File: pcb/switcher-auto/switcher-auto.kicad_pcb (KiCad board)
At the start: 2 copper layers, 151.8 x 46 mm, 26 parts, among them J1 Conn_02x22_Top_Bottom, J10 MD-90SM, J11 MD-90SM, J12 MD-90SM, J13 MD-90SM, J14 MD-90SM, J15 Conn_02x22_Top_Bottom, J2 Conn_02x22_Top_Bottom, J3 Conn_02x22_Top_Bottom, J4 MD-90SM, SW1 SW_Push, SW2 SW_Push, U1 CD74HC4067SM96, U2 CD74HC4067SM96, U3 CD74HC4067SM96, U4 CD74HC4067SM96, U5 CD74HC4067SM96, U6 CD74HC4067SM96, U7 CD74HC4067SM96

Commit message: WIP routing as 4 layers with new connector organization
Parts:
- J1: value Conn_02x22_Top_Bottom -> MD-90SM; footprint connector:REB_PinHeader_2x20_P1.27mm_Vertical_Renumbered -> DIN9:CUI_MD-90SM
- J15: footprint Connector_PinSocket_1.27mm:PinSocket_2x20_P1.27mm_Vertical -> connector:REB_PinHeader_2x20_P1.27mm_Vertical_Renumbered
- J4: value MD-90SM -> Conn_02x22_Top_Bottom; footprint DIN9:CUI_MD-90SM -> connector:REB_PinHeader_2x20_P1.27mm_Vertical_Renumbered
- moved J14 165.4 mm to (210.0, 137.9)
- moved J13 135.8 mm to (180.5, 137.9)
- moved J1 132.8 mm to (211.0, 76.9), turned to 0 degrees
- moved J12 108.7 mm to (151.0, 137.9)
- moved J11 86.3 mm to (121.5, 137.9)
- moved J15 85.3 mm to (137.9, 118.6)
- moved J4 57.1 mm to (164.9, 42.6), turned to 90 degrees
- moved J10 53.4 mm to (92.0, 137.9)
- moved J2 41.6 mm to (83.9, 42.6)
- moved J3 39.5 mm to (124.4, 42.6)
- moved U4 5.36 mm to (179.0, 58.0)
- moved B1 5.22 mm to (215.0, 44.0)
- moved H2 3.58 mm to (75.0, 75.0)
- moved H4 3.54 mm to (225.0, 75.0)
- moved H1 2.17 mm to (75.0, 55.0)
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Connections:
- net /15_5V renamed /15_VCC
- net /SEL_5V renamed /SEL_VCC
- J1 pad 1: /0_BVID -> /SEL_BVID
- J1 pad 2: /0_GVID -> /VCC
- J1 pad 3: /0_RVID -> /SEL_GVID
- J1 pad 4: /0_CVID -> /SEL_CVID
- J1 pad 5: /0_LAUD -> unconnected-(J1-CSYNC-Pad5)
- J1 pad 6: /0_RAUD -> unconnected-(J1-MAUD-Pad6)
- J1 pad 7: /0_5V -> /SEL_RVID
- J1 pad 8: GND -> /SEL_LAUD
- J1 pad 9: /1_BVID -> /SEL_RAUD
- J10 pad 2: /Daughterboard/0_5V -> /Daughterboard/0_VCC
- J11 pad 2: /Daughterboard/1_5V -> /Daughterboard/1_VCC
- J11 pad S1: /Daughterboard/1_GND -> /Daughterboard/0_GND
- J11 pad S2: /Daughterboard/1_GND -> /Daughterboard/0_GND
- J11 pad S3: /Daughterboard/1_GND -> /Daughterboard/0_GND
- J12 pad 2: /Daughterboard/2_5V -> /Daughterboard/2_VCC
- J12 pad S1: /Daughterboard/2_GND -> /Daughterboard/0_GND
- J12 pad S2: /Daughterboard/2_GND -> /Daughterboard/0_GND
- J12 pad S3: /Daughterboard/2_GND -> /Daughterboard/0_GND
- J13 pad 2: /Daughterboard/3_5V -> /Daughterboard/3_VCC
- J13 pad S1: /Daughterboard/3_GND -> /Daughterboard/0_GND
- J13 pad S2: /Daughterboard/3_GND -> /Daughterboard/0_GND
- J13 pad S3: /Daughterboard/3_GND -> /Daughterboard/0_GND
- J14 pad 2: /Daughterboard/4_5V -> /Daughterboard/4_VCC
- J14 pad S1: /Daughterboard/4_GND -> /Daughterboard/0_GND
- J14 pad S2: /Daughterboard/4_GND -> /Daughterboard/0_GND
- J14 pad S3: /Daughterboard/4_GND -> /Daughterboard/0_GND
- J15 pad 1: /Daughterboard/0_BVID -> /Daughterboard/0_RVID
- J15 pad 10: /Daughterboard/1_GVID -> /Daughterboard/4_BVID
- J15 pad 11: /Daughterboard/1_RVID -> /Daughterboard/0_GVID
- J15 pad 12: /Daughterboard/1_CVID -> /Daughterboard/1_GVID
- J15 pad 13: /Daughterboard/1_LAUD -> /Daughterboard/2_GVID
- J15 pad 14: /Daughterboard/1_RAUD -> /Daughterboard/3_GVID
- J15 pad 15: /Daughterboard/1_5V -> /Daughterboard/4_GVID
- J15 pad 16: /Daughterboard/1_GND -> /Daughterboard/0_GND
- J15 pad 17: /Daughterboard/4_BVID -> /Daughterboard/0_GND
- J15 pad 18: /Daughterboard/4_GVID -> /Daughterboard/0_GND
- J15 pad 19: /Daughterboard/4_RVID -> /Daughterboard/0_GND
- J15 pad 2: /Daughterboard/0_GVID -> /Daughterboard/1_RVID
- J15 pad 20: /Daughterboard/4_CVID -> /Daughterboard/0_GND
- J15 pad 21: /Daughterboard/4_LAUD -> /Daughterboard/0_VCC
- J15 pad 22: /Daughterboard/4_RAUD -> /Daughterboard/1_VCC
- J15 pad 23: /Daughterboard/4_5V -> /Daughterboard/2_VCC
- J15 pad 24: /Daughterboard/4_GND -> /Daughterboard/3_VCC
- J15 pad 25: /Daughterboard/3_BVID -> /Daughterboard/4_VCC
- J15 pad 26: /Daughterboard/3_GVID -> /Daughterboard/0_RAUD
- J15 pad 27: /Daughterboard/3_RVID -> /Daughterboard/1_RAUD
- J15 pad 28: /Daughterboard/3_CVID -> /Daughterboard/2_RAUD
- J15 pad 29: /Daughterboard/3_LAUD -> /Daughterboard/3_RAUD
- J15 pad 3: /Daughterboard/0_RVID -> /Daughterboard/2_RVID
- J15 pad 30: /Daughterboard/3_RAUD -> /Daughterboard/4_RAUD
- J15 pad 31: /Daughterboard/3_5V -> /Daughterboard/0_LAUD
- J15 pad 32: /Daughterboard/3_GND -> /Daughterboard/1_LAUD
- J15 pad 33: /Daughterboard/2_BVID -> /Daughterboard/2_LAUD
- J15 pad 34: /Daughterboard/2_GVID -> /Daughterboard/3_LAUD
- J15 pad 35: /Daughterboard/2_RVID -> /Daughterboard/4_LAUD
- J15 pad 36: /Daughterboard/2_CVID -> /Daughterboard/0_CVID
- J15 pad 37: /Daughterboard/2_LAUD -> /Daughterboard/1_CVID
- J15 pad 38: /Daughterboard/2_RAUD -> /Daughterboard/2_CVID
- J15 pad 39: /Daughterboard/2_5V -> /Daughterboard/3_CVID
- J15 pad 4: /Daughterboard/0_CVID -> /Daughterboard/3_RVID
- J15 pad 40: /Daughterboard/2_GND -> /Daughterboard/4_CVID
- J15 pad 5: /Daughterboard/0_LAUD -> /Daughterboard/4_RVID
- J15 pad 6: /Daughterboard/0_RAUD -> /Daughterboard/0_BVID
- J15 pad 7: /Daughterboard/0_5V -> /Daughterboard/1_BVID
- J15 pad 8: /Daughterboard/0_GND -> /Daughterboard/2_BVID
- J15 pad 9: /Daughterboard/1_BVID -> /Daughterboard/3_BVID
- J2 pad 1: /5_BVID -> /0_RVID
- J2 pad 10: /6_GVID -> /4_BVID
- J2 pad 11: /6_RVID -> /0_GVID
- J2 pad 12: /6_CVID -> /1_GVID
- J2 pad 13: /6_LAUD -> /2_GVID
- J2 pad 14: /6_RAUD -> /3_GVID
- J2 pad 15: /6_5V -> /4_GVID
- J2 pad 17: /9_BVID -> GND
- J2 pad 18: /9_GVID -> GND
- J2 pad 19: /9_RVID -> GND
- J2 pad 2: /5_GVID -> /1_RVID
- J2 pad 20: /9_CVID -> GND
- J2 pad 21: /9_LAUD -> /0_VCC
- J2 pad 22: /9_RAUD -> /1_VCC
- J2 pad 23: /9_5V -> /2_VCC
- J2 pad 24: GND -> /3_VCC
- J2 pad 25: /8_BVID -> /4_VCC
- J2 pad 26: /8_GVID -> /0_RAUD
- J2 pad 27: /8_RVID -> /1_RAUD
- J2 pad 28: /8_CVID -> /2_RAUD
- J2 pad 29: /8_LAUD -> /3_RAUD
- J2 pad 3: /5_RVID -> /2_RVID
- J2 pad 30: /8_RAUD -> /4_RAUD
- J2 pad 31: /8_5V -> /0_LAUD
- J2 pad 32: GND -> /1_LAUD
- J2 pad 33: /7_BVID -> /2_LAUD
- J2 pad 34: /7_GVID -> /3_LAUD
- J2 pad 35: /7_RVID -> /4_LAUD
- J2 pad 36: /7_CVID -> /0_CVID
- J2 pad 37: /7_LAUD -> /1_CVID
- J2 pad 38: /7_RAUD -> /2_CVID
- J2 pad 39: /7_5V -> /3_CVID
- J2 pad 4: /5_CVID -> /3_RVID
- J2 pad 40: GND -> /4_CVID
- J2 pad 5: /5_LAUD -> /4_RVID
- J2 pad 6: /5_RAUD -> /0_BVID
- J2 pad 7: /5_5V -> /1_BVID
- J2 pad 8: GND -> /2_BVID
- J2 pad 9: /6_BVID -> /3_BVID
- J3 pad 1: /10_BVID -> /5_RVID
- J3 pad 10: /11_GVID -> /9_BVID
- J3 pad 11: /11_RVID -> /5_GVID
- J3 pad 12: /11_CVID -> /6_GVID
- J3 pad 13: /11_LAUD -> /7_GVID
- J3 pad 14: /11_RAUD -> /8_GVID
- J3 pad 15: /11_5V -> /9_GVID
- J3 pad 17: /14_BVID -> GND
- J3 pad 18: /14_GVID -> GND
- J3 pad 19: /14_RVID -> GND
- J3 pad 2: /10_GVID -> /6_RVID
- J3 pad 20: /14_CVID -> GND
- J3 pad 21: /14_LAUD -> /5_VCC
- J3 pad 22: /14_RAUD -> /6_VCC
- J3 pad 23: /14_5V -> /7_VCC
- J3 pad 24: GND -> /8_VCC
- J3 pad 25: /13_BVID -> /9_VCC
- J3 pad 26: /13_GVID -> /5_RAUD
- J3 pad 27: /13_RVID -> /6_RAUD
- J3 pad 28: /13_CVID -> /7_RAUD
- J3 pad 29: /13_LAUD -> /8_RAUD
- J3 pad 3: /10_RVID -> /7_RVID
- J3 pad 30: /13_RAUD -> /9_RAUD
- J3 pad 31: /13_5V -> /5_LAUD
- J3 pad 32: GND -> /6_LAUD
- J3 pad 33: /12_BVID -> /7_LAUD
- J3 pad 34: /12_GVID -> /8_LAUD
- J3 pad 35: /12_RVID -> /9_LAUD
- J3 pad 36: /12_CVID -> /5_CVID
- J3 pad 37: /12_LAUD -> /6_CVID
- J3 pad 38: /12_RAUD -> /7_CVID
- J3 pad 39: /12_5V -> /8_CVID
- J3 pad 4: /10_CVID -> /8_RVID
- J3 pad 40: GND -> /9_CVID
- J3 pad 5: /10_LAUD -> /9_RVID
- J3 pad 6: /10_RAUD -> /5_BVID
- J3 pad 7: /10_5V -> /6_BVID
- J3 pad 8: GND -> /7_BVID
- J3 pad 9: /11_BVID -> /8_BVID
- J4 pad 1: /SEL_BVID -> /10_RVID
- J4 pad 2: /VCC -> /11_RVID
- J4 pad 3: /SEL_GVID -> /12_RVID
- J4 pad 4: /SEL_CVID -> /13_RVID
- J4 pad 5: unconnected-(J4-CSYNC-Pad5) -> /14_RVID
- J4 pad 6: unconnected-(J4-MAUD-Pad6) -> /10_BVID
- J4 pad 7: /SEL_RVID -> /11_BVID
- J4 pad 8: /SEL_LAUD -> /12_BVID
- J4 pad 9: /SEL_RAUD -> /13_BVID
- U1 pad 1: /SEL_BVID -> /SEL_RVID
- U1 pad 16: /15_BVID -> /15_RVID
- U1 pad 17: /14_BVID -> /14_RVID
- U1 pad 18: /13_BVID -> /13_RVID
- U1 pad 19: /12_BVID -> /12_RVID
- U1 pad 2: /7_BVID -> /7_RVID
- U1 pad 20: /11_BVID -> /11_RVID
- U1 pad 21: /10_BVID -> /10_RVID
- U1 pad 22: /9_BVID -> /9_RVID
- U1 pad 23: /8_BVID -> /8_RVID
- U1 pad 3: /6_BVID -> /6_RVID
- U1 pad 4: /5_BVID -> /5_RVID
- U1 pad 5: /4_BVID -> /4_RVID
- U1 pad 6: /3_BVID -> /3_RVID
- U1 pad 7: /2_BVID -> /2_RVID
- U1 pad 8: /1_BVID -> /1_RVID
- U1 pad 9: /0_BVID -> /0_RVID
- U2 pad 1: /SEL_GVID -> /SEL_BVID
- U2 pad 16: /15_GVID -> /15_BVID
- U2 pad 17: /14_GVID -> /14_BVID
- U2 pad 18: /13_GVID -> /13_BVID
- U2 pad 19: /12_GVID -> /12_BVID
- U2 pad 2: /7_GVID -> /7_BVID
- U2 pad 20: /11_GVID -> /11_BVID
- U2 pad 21: /10_GVID -> /10_BVID
- U2 pad 22: /9_GVID -> /9_BVID
- U2 pad 23: /8_GVID -> /8_BVID
- U2 pad 3: /6_GVID -> /6_BVID
- U2 pad 4: /5_GVID -> /5_BVID
- U2 pad 5: /4_GVID -> /4_BVID
- U2 pad 6: /3_GVID -> /3_BVID
- U2 pad 7: /2_GVID -> /2_BVID
- U2 pad 8: /1_GVID -> /1_BVID
- U2 pad 9: /0_GVID -> /0_BVID
- U3 pad 1: /SEL_RVID -> /SEL_GVID
- U3 pad 16: /15_RVID -> /15_GVID
- U3 pad 17: /14_RVID -> /14_GVID
- U3 pad 18: /13_RVID -> /13_GVID
- U3 pad 19: /12_RVID -> /12_GVID
- U3 pad 2: /7_RVID -> /7_GVID
- U3 pad 20: /11_RVID -> /11_GVID
- U3 pad 21: /10_RVID -> /10_GVID
- U3 pad 22: /9_RVID -> /9_GVID
- U3 pad 23: /8_RVID -> /8_GVID
- U3 pad 3: /6_RVID -> /6_GVID
- U3 pad 4: /5_RVID -> /5_GVID
- U3 pad 5: /4_RVID -> /4_GVID
- U3 pad 6: /3_RVID -> /3_GVID
- U3 pad 7: /2_RVID -> /2_GVID
- U3 pad 8: /1_RVID -> /1_GVID
- U3 pad 9: /0_RVID -> /0_GVID
- U7 pad 17: /14_5V -> /14_VCC
- U7 pad 18: /13_5V -> /13_VCC
- U7 pad 19: /12_5V -> /12_VCC
- U7 pad 2: /7_5V -> /7_VCC
- U7 pad 20: /11_5V -> /11_VCC
- U7 pad 21: /10_5V -> /10_VCC
- U7 pad 22: /9_5V -> /9_VCC
- U7 pad 23: /8_5V -> /8_VCC
- U7 pad 3: /6_5V -> /6_VCC
- U7 pad 4: /5_5V -> /5_VCC
- U7 pad 5: /4_5V -> /4_VCC
- U7 pad 6: /3_5V -> /3_VCC
- U7 pad 7: /2_5V -> /2_VCC
- U7 pad 8: /1_5V -> /1_VCC
- U7 pad 9: /0_5V -> /0_VCC
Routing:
- net /OE: track 0.00 -> 179.0 mm, vias 0 -> 4
- net /S0: track 0.00 -> 151.7 mm, vias 0 -> 2
- net /S2: track 0.00 -> 147.8 mm, vias 0 -> 2
- net /S1: track 0.00 -> 146.7 mm, vias 0 -> 2
- net /S3: track 0.00 -> 135.8 mm, vias 0 -> 3
- net /4_CVID: track 0.00 -> 107.2 mm, vias 0 -> 1
- net /10_LAUD: track 0.00 -> 107.1 mm, vias 0 -> 2
- net /3_CVID: track 0.00 -> 106.5 mm, vias 0 -> 1
- net /11_LAUD: track 0.00 -> 106.2 mm, vias 0 -> 2
- net /2_CVID: track 0.00 -> 105.7 mm, vias 0 -> 1
- net /12_LAUD: track 0.00 -> 105.2 mm, vias 0 -> 2
- net /1_CVID: track 0.00 -> 104.9 mm, vias 0 -> 1
- net /0_CVID: track 0.00 -> 104.2 mm, vias 0 -> 1
- net /13_LAUD: track 0.00 -> 104.0 mm, vias 0 -> 2
- net /14_LAUD: track 0.00 -> 102.9 mm, vias 0 -> 2
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- added copper zone on B.Cu, net /Daughterboard/0_GND
- added copper zone on F.Cu, net /Daughterboard/0_GND
- removed copper zone on B.Cu, net GND
- removed copper zone on F.Cu, net GND
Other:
- board size 151.8 x 46 mm -> 160 x 110 mm
- copper layers 2 -> 4

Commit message: Routing pt 2
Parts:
- added C1: 1u, Capacitor_SMD:C_0805_2012Metric_Pad1.18x1.45mm_HandSolder, F.Cu at (220.0, 63.0)
- added R3: R_Small, Resistor_SMD:R_1206_3216Metric_Pad1.30x1.75mm_HandSolder, F.Cu at (163.2, 130.8)
- added R4: R_Small, Resistor_SMD:R_1206_3216Metric_Pad1.30x1.75mm_HandSolder, F.Cu at (133.6, 130.8)
- added R5: R_Small, Resistor_SMD:R_1206_3216Metric_Pad1.30x1.75mm_HandSolder, F.Cu at (104.4, 130.8)
- added R6: 10K, Resistor_SMD:R_1206_3216Metric_Pad1.30x1.75mm_HandSolder, F.Cu at (209.9, 56.4)
- R1: value R -> R_Small
- R2: value 10K -> R_Small
- moved R1 75.8 mm to (222.2, 130.8), turned to 90 degrees
- moved R2 69.6 mm to (192.6, 130.8), turned to 90 degrees
- moved SW1 1.35 mm to (190.2, 73.0)
- moved SW2 1.27 mm to (179.5, 73.0)
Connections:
- B1 pad 17: unconnected-(B1-A0-Pad17) -> /SEL_VCC
- B1 pad 2: /OE -> unconnected-(B1-RXI-Pad2)
- B1 pad 5: /R0 -> /R1
- B1 pad 6: /R1 -> /R0
- B1 pad 7: /R2 -> /R3
- B1 pad 8: /R3 -> /R2
- B1 pad 9: Net-(B1-*6) -> unconnected-(B1-*6-Pad9)
- R1 pad 1: /SEL_VCC -> /Daughterboard/4_VCC
- R1 pad 2: Net-(B1-*6) -> unconnected-(R1-Pad2)
- R2 pad 1: Net-(B1-*6) -> /Daughterboard/3_VCC
- R2 pad 2: GND -> unconnected-(R2-Pad2)
- U1 pad 15: /OE -> GND
- U1 pad 16: /15_RVID -> unconnected-(U1-I15-Pad16)
- U2 pad 15: /OE -> GND
- U2 pad 16: /15_BVID -> unconnected-(U2-I15-Pad16)
- U3 pad 15: /OE -> GND
- U3 pad 16: /15_GVID -> unconnected-(U3-I15-Pad16)
- U4 pad 15: /OE -> GND
- U4 pad 16: /15_CVID -> unconnected-(U4-I15-Pad16)
- U5 pad 15: /OE -> GND
- U5 pad 16: /15_LAUD -> unconnected-(U5-I15-Pad16)
- U6 pad 15: /OE -> GND
- U6 pad 16: /15_RAUD -> unconnected-(U6-I15-Pad16)
- U7 pad 16: /15_VCC -> unconnected-(U7-I15-Pad16)
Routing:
- net /VCC: track 0.00 -> 288.8 mm, vias 0 -> 3
- net /OE: track 179.0 -> 0.00 mm, vias 4 -> 0
- net /SEL_RVID: track 0.00 -> 158.9 mm, vias 0 -> 1
- net /SEL_LAUD: track 0.00 -> 118.3 mm, vias 0 -> 1
- net /SEL_BVID: track 0.00 -> 113.6 mm, vias 0 -> 1
- net /SEL_GVID: track 0.00 -> 96.2 mm, vias 0 -> 1
- net /SEL_RAUD: track 0.00 -> 86.9 mm, vias 0 -> 1
- net /IE: track 0.00 -> 84.7 mm, vias 0 -> 1
- net /R1: track 0.00 -> 81.1 mm, vias 0 -> 1
- net /R0: track 0.00 -> 78.6 mm, vias 0 -> 1
- net /10_RAUD: track 0.00 -> 78.0 mm, vias 0 -> 1
- net /11_RAUD: track 0.00 -> 76.6 mm, vias 0 -> 1
- net /12_RAUD: track 0.00 -> 75.4 mm, vias 0 -> 1
- net /4_VCC: track 0.00 -> 74.9 mm, vias 0 -> 1
- net /13_RAUD: track 0.00 -> 74.0 mm, vias 0 -> 1
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- added copper zone on In2.Cu, net GND

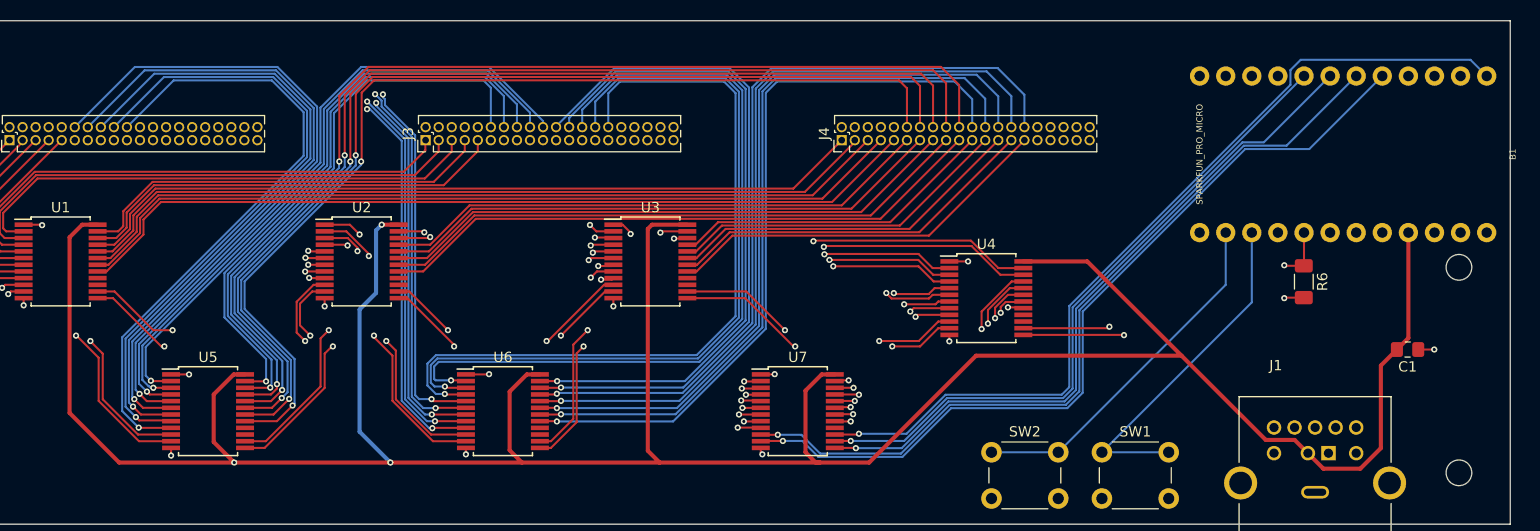
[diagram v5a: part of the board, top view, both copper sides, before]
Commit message: Finish routing, not done with daughterboard changes
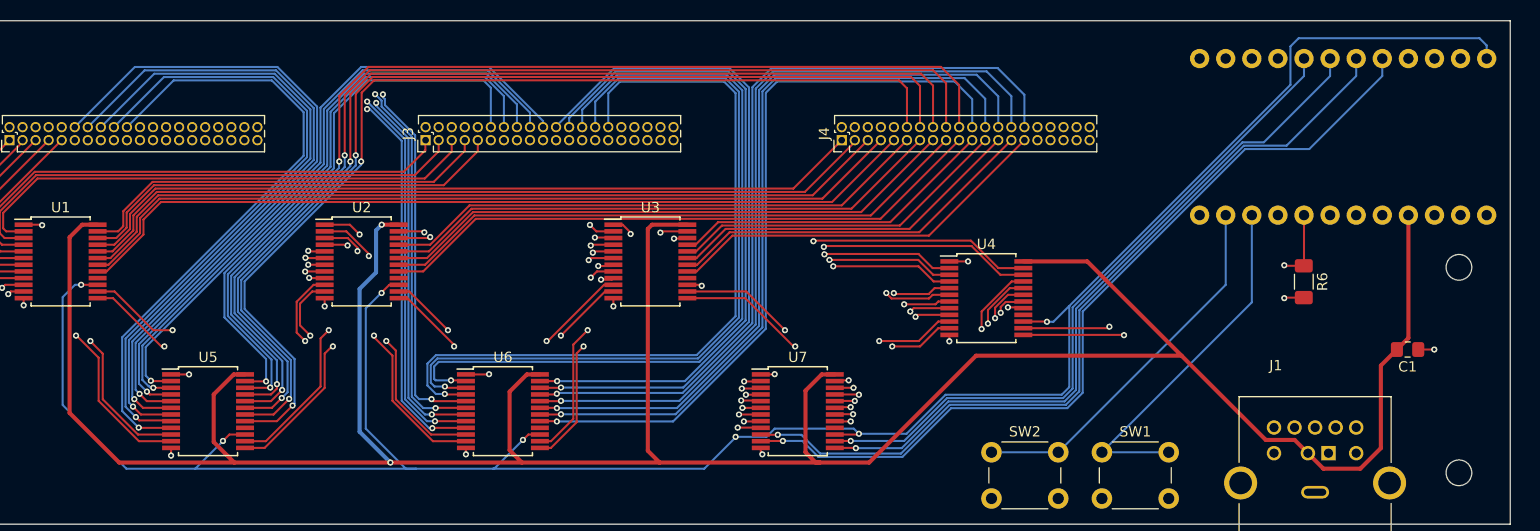
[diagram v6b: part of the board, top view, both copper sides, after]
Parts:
- B1: value SPARKFUN_PRO_MICRO -> >VALUE
- moved B1 1.70 mm to (215.0, 42.3)
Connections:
- B1 pad 1: /IE -> /EN
- U1 pad 15: GND -> /EN
- U2 pad 15: GND -> /EN
- U3 pad 15: GND -> /EN
- U4 pad 15: GND -> /EN
- U5 pad 15: GND -> /EN
- U6 pad 15: GND -> /EN
- U7 pad 15: /IE -> /EN
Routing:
- net /EN: track 0.00 -> 241.7 mm, vias 0 -> 8
- net /IE: track 84.7 -> 0.00 mm, vias 1 -> 0
- net /S0: track 200.8 -> 202.5 mm
- net /S1: track 195.9 -> 197.6 mm
- net /R1: track 81.1 -> 82.8 mm
- net /R3: track 67.9 -> 69.6 mm
- net /R2: track 65.0 -> 66.7 mm
- net /R0: track 78.6 -> 80.3 mm
- net Net-(B1-12(MISO)): track 33.9 -> 35.6 mm
- net Net-(B1-11(MOSI)): track 34.6 -> 36.3 mm
- net /VCC: track 288.8 -> 290.5 mm, vias 3 -> 2
- net /SEL_VCC: track 63.6 -> 65.3 mm
- net /S3: track 174.9 -> 176.6 mm
- net /S2: track 186.0 -> 187.6 mm

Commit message: finish routing?
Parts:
- added H10: MountingHole, MountingHole:MountingHole_2.5mm, F.Cu at (75.0, 116.0)
- added H12: MountingHole, MountingHole:MountingHole_2.5mm, F.Cu at (75.0, 136.0)
- added H13: MountingHole, MountingHole:MountingHole_2.5mm, F.Cu at (225.0, 116.0)
- added H14: MountingHole, MountingHole:MountingHole_2.5mm, F.Cu at (225.0, 136.0)
- B1: value >VALUE -> SPARKFUN_PRO_MICRO
- moved R4 0.70 mm to (134.3, 130.8), turned to -90 degrees
- turned R1 to -90 degrees
- turned R2 to -90 degrees
- turned R3 to -90 degrees
- turned R5 to -90 degrees
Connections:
- J15 pad 21: /Daughterboard/0_VCC -> Net-(J15-Pin_21)
- J15 pad 22: /Daughterboard/1_VCC -> Net-(J15-Pin_22)
- J15 pad 23: /Daughterboard/2_VCC -> Net-(J15-Pin_23)
- J15 pad 24: /Daughterboard/3_VCC -> Net-(J15-Pin_24)
- J15 pad 25: /Daughterboard/4_VCC -> Net-(J15-Pin_25)
- R1 pad 1: /Daughterboard/4_VCC -> Net-(J15-Pin_25)
- R1 pad 2: unconnected-(R1-Pad2) -> /Daughterboard/4_VCC
- R2 pad 1: /Daughterboard/3_VCC -> Net-(J15-Pin_24)
- R2 pad 2: unconnected-(R2-Pad2) -> /Daughterboard/3_VCC
- R3 pad 1: /Daughterboard/2_VCC -> Net-(J15-Pin_23)
- R3 pad 2: unconnected-(R3-Pad2) -> /Daughterboard/2_VCC
- R4 pad 1: /Daughterboard/1_VCC -> Net-(J15-Pin_22)
- R4 pad 2: unconnected-(R4-Pad2) -> /Daughterboard/1_VCC
- R5 pad 1: /Daughterboard/0_VCC -> Net-(J15-Pin_21)
- R5 pad 2: unconnected-(R5-Pad2) -> /Daughterboard/0_VCC
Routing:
- net Net-(J15-Pin_25): track 0.00 -> 74.9 mm
- net /Daughterboard/4_VCC: track 83.9 -> 14.7 mm
- net Net-(J15-Pin_21): track 0.00 -> 68.2 mm, vias 0 -> 1
- net /Daughterboard/0_VCC: track 83.3 -> 15.2 mm
- net Net-(J15-Pin_22): track 0.00 -> 46.4 mm, vias 0 -> 1
- net Net-(J15-Pin_24): track 0.00 -> 44.5 mm, vias 0 -> 2
- net /Daughterboard/1_VCC: track 57.8 -> 15.6 mm
- net Net-(J15-Pin_23): track 0.00 -> 26.6 mm, vias 0 -> 2
- net /Daughterboard/2_VCC: track 39.0 -> 15.1 mm, vias 1 -> 0
- net /Daughterboard/3_VCC: track 38.2 -> 14.8 mm, vias 1 -> 0
- net /10_RAUD: track 78.0 -> 70.5 mm
- net /11_RAUD: track 76.6 -> 69.2 mm
- net /12_RAUD: track 75.4 -> 68.0 mm
- net /13_RAUD: track 74.0 -> 66.7 mm
- net /14_RAUD: track 72.7 -> 65.5 mm
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
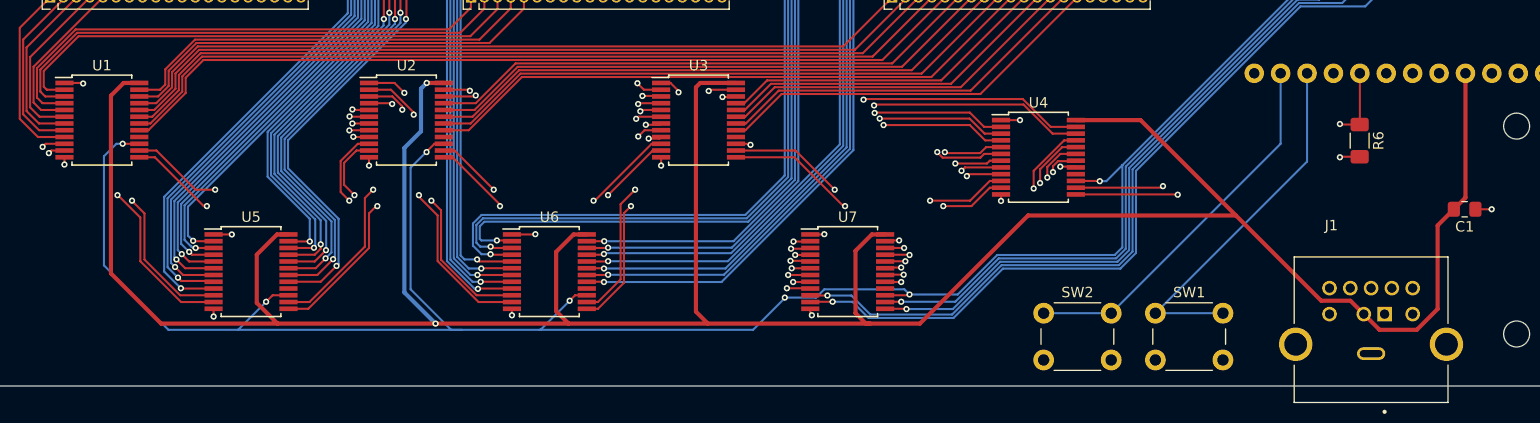
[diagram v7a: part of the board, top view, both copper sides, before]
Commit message: decouple every mux
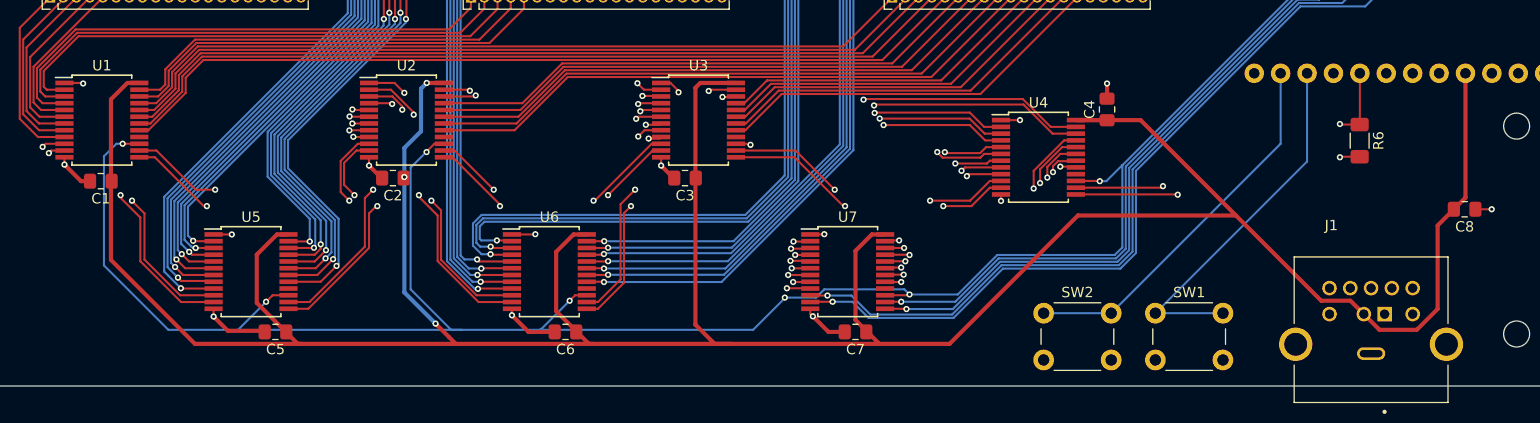
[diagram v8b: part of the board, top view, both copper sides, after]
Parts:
- added C1: 0.1u, Capacitor_SMD:C_0805_2012Metric_Pad1.18x1.45mm_HandSolder, F.Cu at (88.8, 60.3)
- added C2: 0.1u, Capacitor_SMD:C_0805_2012Metric_Pad1.18x1.45mm_HandSolder, F.Cu at (116.9, 60.0)
- added C3: 0.1u, Capacitor_SMD:C_0805_2012Metric_Pad1.18x1.45mm_HandSolder, F.Cu at (145.0, 60.0)
- added C4: 0.1u, Capacitor_SMD:C_0805_2012Metric_Pad1.18x1.45mm_HandSolder, F.Cu at (185.6, 53.4)
- added C5: 0.1u, Capacitor_SMD:C_0805_2012Metric_Pad1.18x1.45mm_HandSolder, F.Cu at (105.6, 74.8)
- added C6: 0.1u, Capacitor_SMD:C_0805_2012Metric_Pad1.18x1.45mm_HandSolder, F.Cu at (133.5, 74.8)
- added C7: 0.1u, Capacitor_SMD:C_0805_2012Metric_Pad1.18x1.45mm_HandSolder, F.Cu at (161.4, 74.8)
- renumbered C1 to C8, H10 to H1, H12 to H2, H13 to H3, H14 to H4
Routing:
- net GND: track 8.47 -> 30.7 mm, vias 9 -> 10
- net /VCC: track 290.5 -> 309.0 mm, vias 2 -> 3
- net /SEL_GVID: track 96.2 -> 98.5 mm
- net /SEL_LAUD: track 118.3 -> 119.3 mm
- net /SEL_RAUD: track 86.9 -> 87.9 mm
- net /SEL_BVID: track 113.6 -> 114.6 mm
- net /SEL_RVID: track 159.6 -> 160.6 mm
